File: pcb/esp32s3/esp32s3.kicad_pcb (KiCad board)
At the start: 4 copper layers, 59.7 x 58.9 mm, 82 parts, among them J1 USB_C_Receptacle_USB2.0_14P, J2 Battery, J3 GPS_ANT, J4 Conn_Coaxial, J5 Conn_01x40_Socket, Q1 DMG3414U, Q1_Xtal1 32.0MHz, Q3 DMG1012T, SW1 BOOT, SW2 PTS815 SJM 250 SMTR LFS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

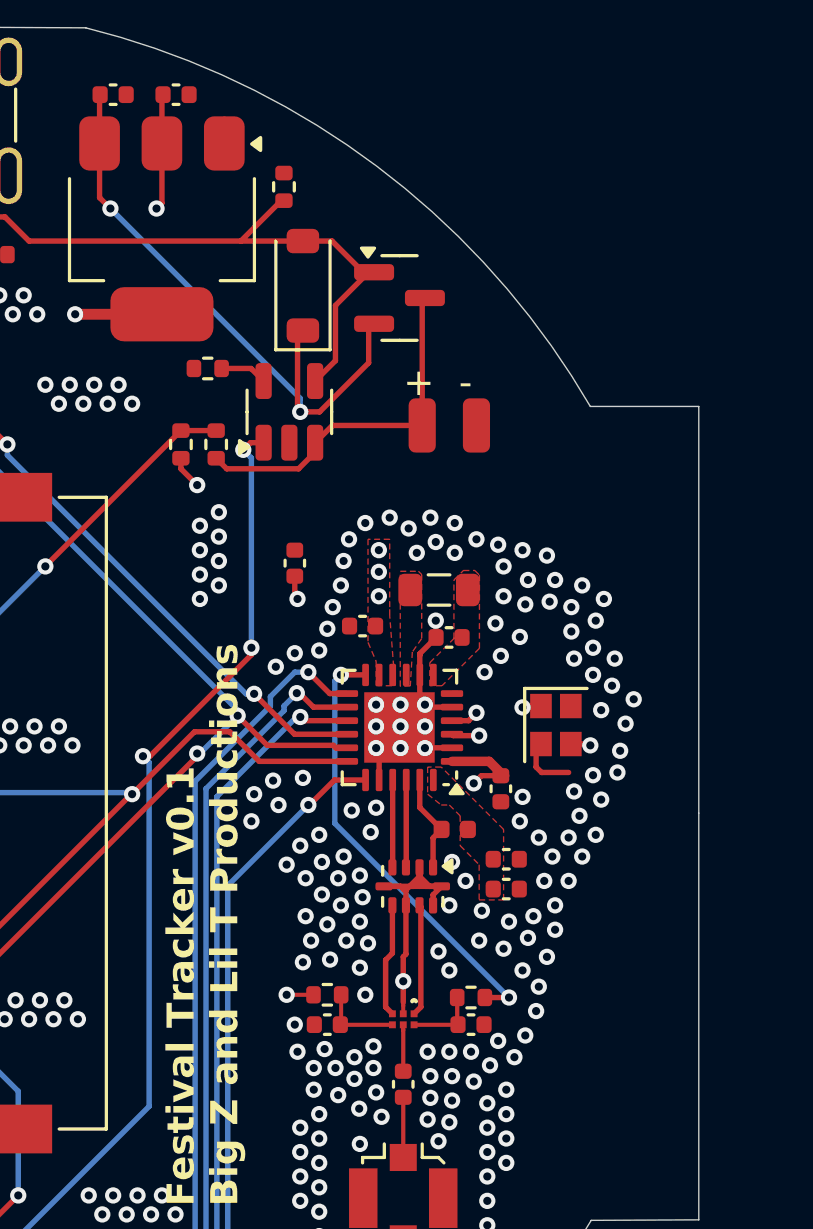
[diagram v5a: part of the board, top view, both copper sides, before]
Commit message: fix power circuit
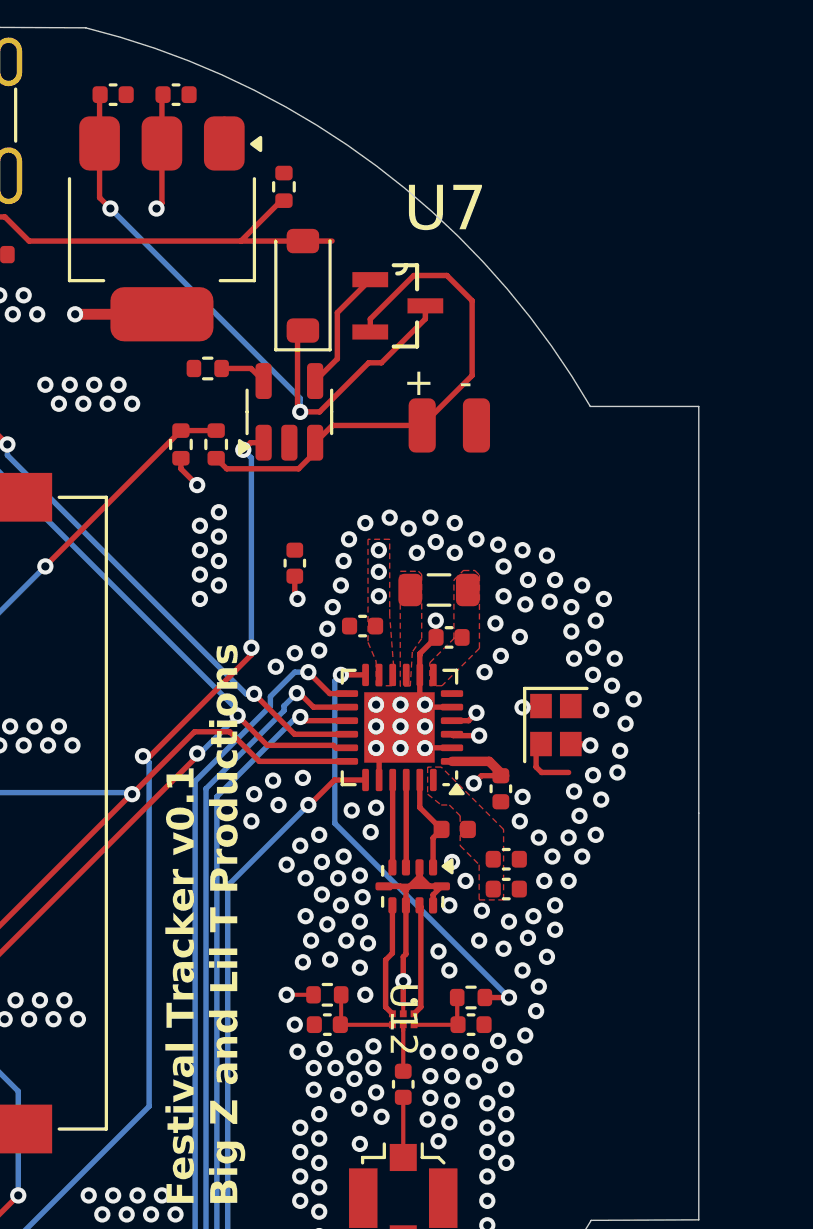
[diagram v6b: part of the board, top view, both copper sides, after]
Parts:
- removed Q1: DMG3414U, Package_TO_SOT_SMD:SOT-23
- added U7: DMG3415U-7, DMG3415:SOT95P240X105-3N, F.Cu at (148.7, 53.3)
- U12: footprint custom_comps:TSNP-6-2&slash_-8_INF -> BGS12SN6:TSNP-6-2&slash_-8_INF
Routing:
- net +BATT: track 13.4 -> 19.3 mm
- net VBUS: track 36.2 -> 34.3 mm
- net VCC: track 22.5 -> 24.3 mm

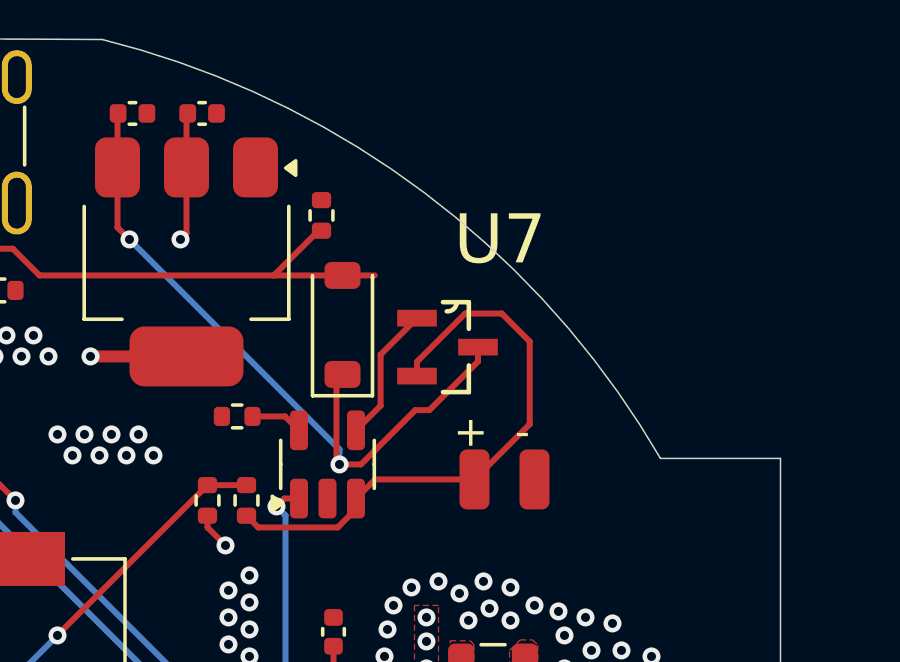
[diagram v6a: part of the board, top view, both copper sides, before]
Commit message: changed so exact same mosfet placement
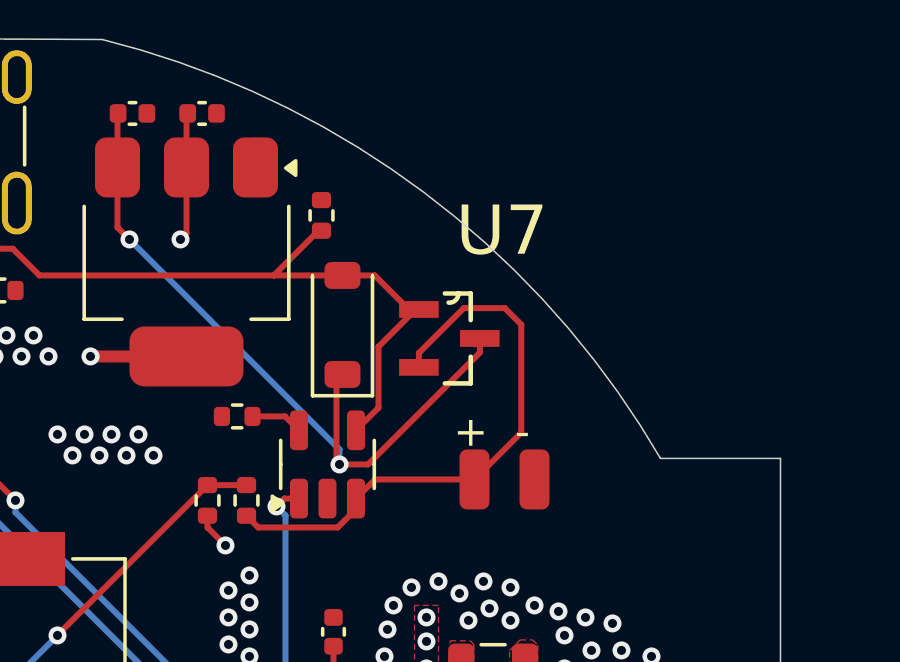
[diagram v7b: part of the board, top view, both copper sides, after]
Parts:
- moved U7 0.30 mm to (148.8, 53.0)
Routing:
- net VBUS: track 34.3 -> 36.2 mm
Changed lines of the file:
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@@
 	(footprint "DMG3415:SOT95P240X105-3N"
 		(layer "F.Cu")
-		(at 148.7 53.29)
+		(at 148.7625 53)
 		(property "Reference" "U7"
 			(at 1.753325 -3.582895 0)
@@
 	)
 	(segment
-		(start 149.716 53.7694)
-		(end 149.716 53.29)
+		(start 149.5 53)
+		(end 149.5 53.1)
 		(width 0.2)
 		(layer "F.Cu")
@@
 	)
 	(segment
-		(start 145.815552 57.2)
-		(end 147.625 55.390552)
+		(start 149.5 53.1)
+		(end 149.6 53.2)
 		(width 0.2)
 		(layer "F.Cu")
@@
 	)
 	(segment
-		(start 147.625 55.390552)
-		(end 148.094848 55.390552)
+		(start 149.7785 53.473)
+		(end 149.7785 53)
+		(width 0.2)
+		(layer "F.Cu")
+		(net 14)
+	)
+	(segment
+		(start 145.1 57.2)
+		(end 146.0515 57.2)
 		(width 0.2)
 		(layer "F.Cu")
@@
 	)
 	(segment
-		(start 148.094848 55.390552)
-		(end 149.716 53.7694)
-		(width 0.2)
-		(layer "F.Cu")
-		(net 14)
-	)
-	(segment
 		(start 137.7 45.52)
 		(end 137.72 45.5)
@@
 	)
 	(segment
-		(start 145.1 57.2)
-		(end 145.815552 57.2)
+		(start 146.0515 57.2)
+		(end 149.7785 53.473)
 		(width 0.2)
 		(layer "F.Cu")
@@
 	)
 	(segment
-		(start 146.47 53.5388)
-		(end 146.47 55.2425)
-		(width 0.2)
-		(layer "F.Cu")
-		(net 18)
-	)
-	(segment
-		(start 146.47 55.2425)
-		(end 145.65 56.0625)
+		(start 146.4 53.275)
+		(end 146.4 55.3125)
 		(width 0.2)
 		(layer "F.Cu")
@@
 	)
 	(segment
+		(start 146.4 55.3125)
+		(end 145.65 56.0625)
+		(width 0.2)
+		(layer "F.Cu")
+		(net 18)
+	)
+	(segment
 		(start 127.825 48.89)
 		(end 127.825 48.17)
@@
 	)
 	(segment
+		(start 147.625 52.05)
+		(end 146.4 53.275)
+		(width 0.2)
+		(layer "F.Cu")
+		(net 18)
+	)
+	(segment
+		(start 146.275 50.9)
+		(end 147.425 52.05)
+		(width 0.2)
+		(layer "F.Cu")
+		(net 18)
+	)
+	(segment
 		(start 131.140552 52.4875)
 		(end 130.150001 52.4875)
@@
 	)
 	(segment
-		(start 147.684 52.3248)
-		(end 146.47 53.5388)
-		(width 0.2)
-		(layer "F.Cu")
-		(net 18)
-	)
-	(segment
 		(start 131.5 50.2)
 		(end 131.275 49.975)
@@
 	)
 	(segment
-		(start 150.51 52.17)
-		(end 151.44 53.1)
+		(start 147.7465 53.4858)
+		(end 149.2423 51.99)
 		(width 0.2)
 		(layer "F.Cu")
@@
 	)
 	(segment
-		(start 149.2898 52.17)
-		(end 150.51 52.17)
-		(width 0.2)
-		(layer "F.Cu")
-		(net 24)
-	)
-	(segment
-		(start 151.44 53.1)
-		(end 151.44 55.86)
-		(width 0.2)
-		(layer "F.Cu")
-		(net 24)
-	)
-	(segment
-		(start 151.44 55.86)
+		(start 151.16 56.14)
 		(end 149.6 57.7)
 		(width 0.2)
@@
 	)
 	(segment
-		(start 147.684 54.2552)
-		(end 147.684 53.7758)
+		(start 150.61 51.99)
+		(end 151.16 52.54)
 		(width 0.2)
 		(layer "F.Cu")
@@
 	)
 	(segment
-		(start 147.684 53.7758)
-		(end 149.2898 52.17)
+		(start 151.16 52.54)
+		(end 151.16 56.14)
 		(width 0.2)
 		(layer "F.Cu")
@@
 		(width 0.2)
 		(layer "F.Cu")
+		(net 24)
+	)
+	(segment
+		(start 147.7465 53.9652)
+		(end 147.7465 53.4858)
+		(width 0.2)
+		(layer "F.Cu")
+		(net 24)
+	)
+	(segment
+		(start 149.2423 51.99)
+		(end 150.61 51.99)
+		(width 0.2)
+		(layer "F.Cu")

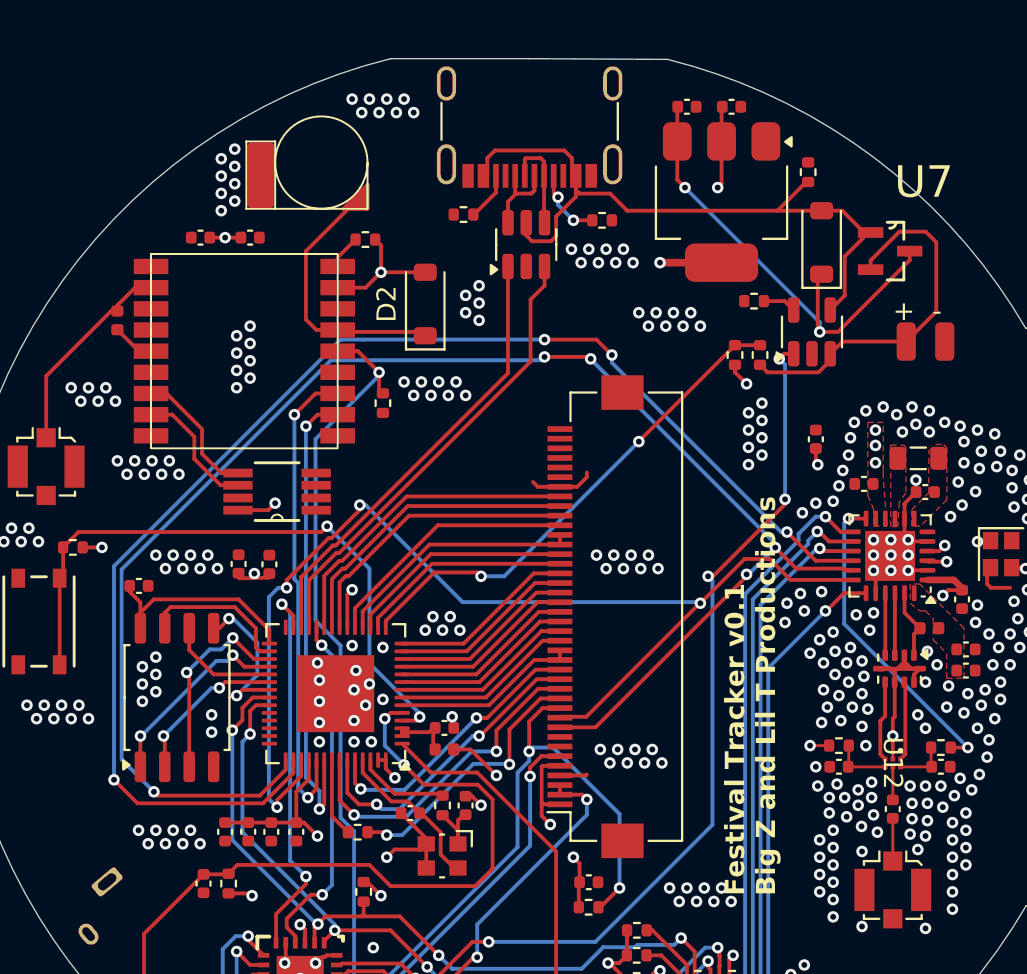
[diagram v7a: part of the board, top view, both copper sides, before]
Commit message: moved display connector to correct position
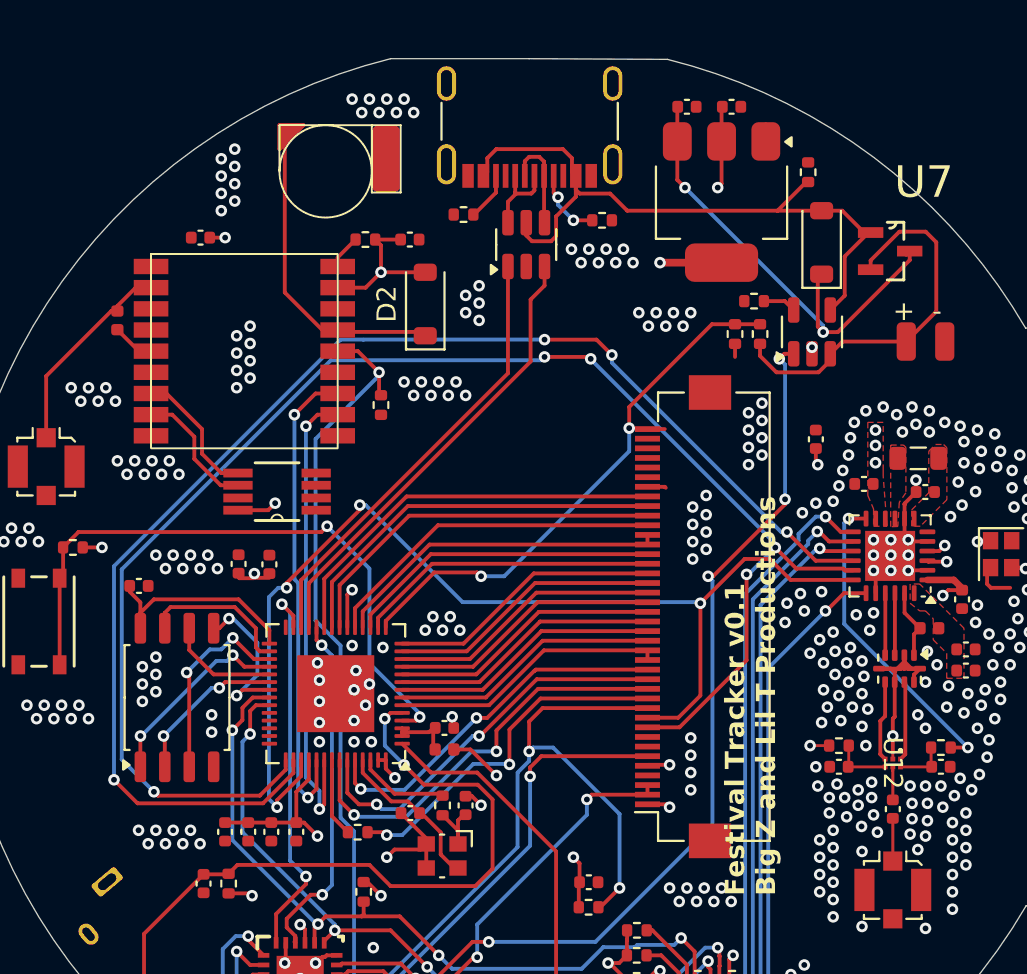
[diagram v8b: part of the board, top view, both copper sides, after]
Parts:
- moved C16 8.30 mm to (123.8, 52.4)
- moved J5 4.55 mm to (138.0, 72.0)
- moved R10 1.09 mm to (142.0, 57.3)
- moved R11 1.09 mm to (140.7, 57.3)
- moved BT1 0.51 mm to (119.4, 48.9), turned to 90 degrees
- moved R4 0.14 mm to (122.3, 61.0)
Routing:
- net LCD_B1: track 9.67 -> 14.4 mm
- net LCD_R1: track 13.0 -> 17.8 mm
- net LCD_VSYNC: track 15.9 -> 20.4 mm
- net Net-(J5-Pin_12): track 14.1 -> 18.6 mm
- net LCD_RST: track 24.4 -> 28.9 mm
- net LCD_R2: track 13.4 -> 18.0 mm
- net LCD_HSYNC: track 14.6 -> 19.1 mm
- net LCD_G5: track 11.8 -> 16.4 mm
- net LCD_G4: track 11.1 -> 15.7 mm
- net LCD_G3: track 9.71 -> 14.3 mm
- net LCD_G2: track 9.67 -> 14.2 mm
- net LCD_G1: track 9.63 -> 14.2 mm
- net LCD_G0: track 9.59 -> 14.1 mm
- net LCD_CS: track 38.0 -> 42.5 mm
- net LCD_B5: track 9.55 -> 14.1 mm
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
